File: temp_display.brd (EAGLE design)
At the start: 101.6 x 76.2 mm, 66 parts, among them IC2 ATMEGA168PROUND, Q1 2N2907, T1 BC547

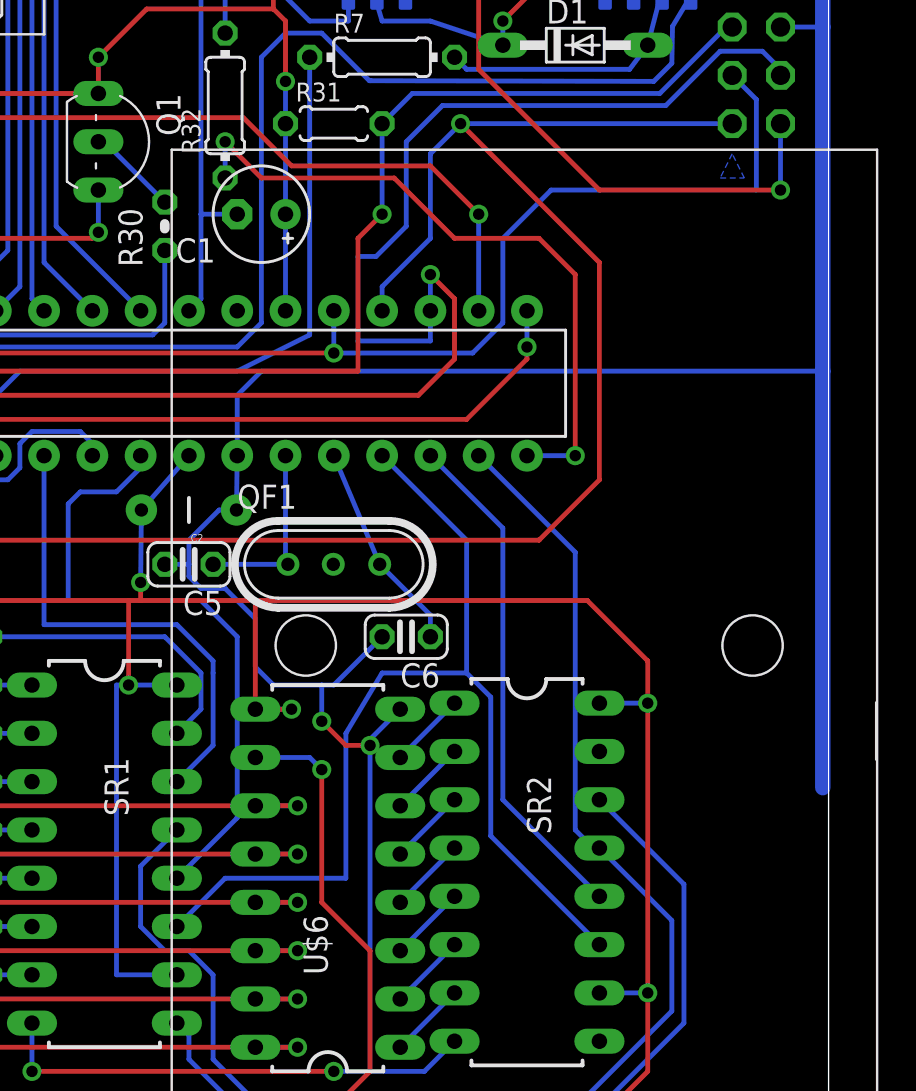
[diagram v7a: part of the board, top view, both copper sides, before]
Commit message: Now shutting down the display during isploading. But the system isn't stable anymore.
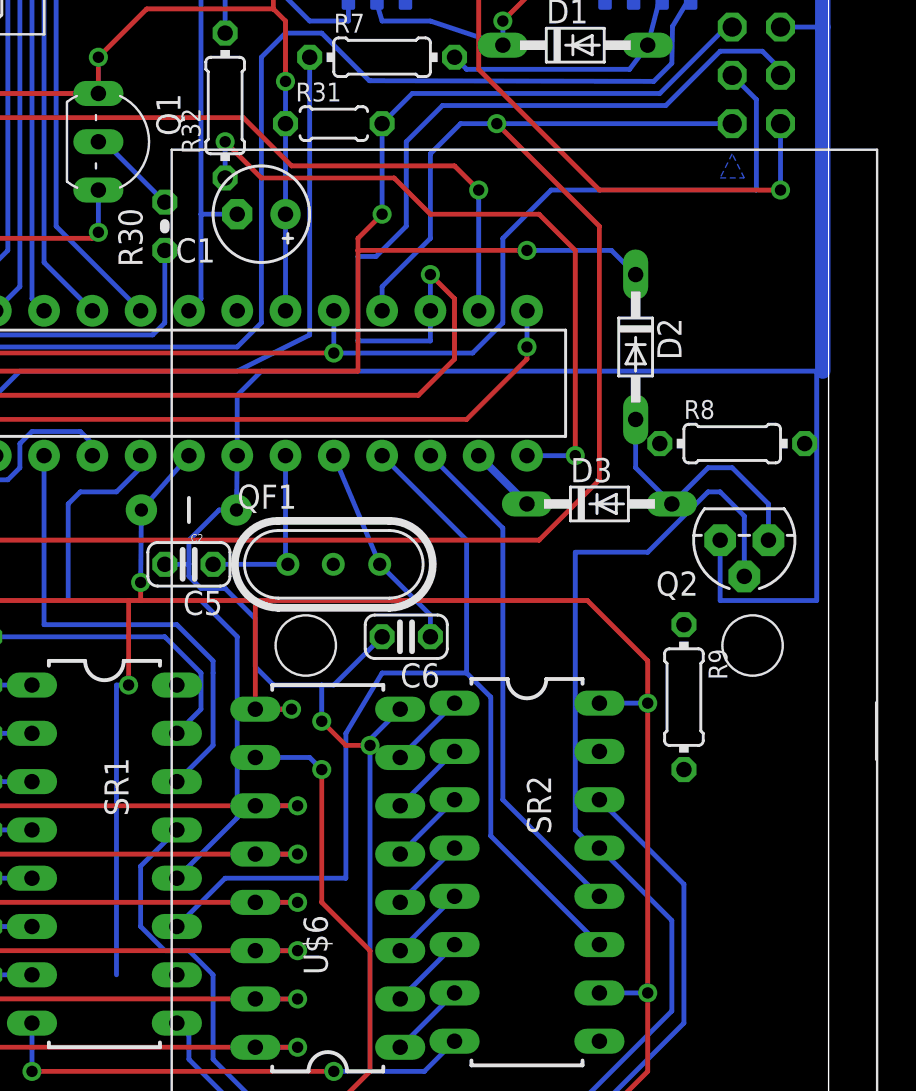
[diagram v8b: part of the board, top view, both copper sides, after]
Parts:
- added D2, D3: BAS15, diode:DO34-7
- added Q2: FQN1N50C, adafruit:TO92
- added R8, R9: 10K, resistor:0204/7
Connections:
- new net N$13: D3.C, IC2.13
- new net N$14: D2.A, D3.A, Q2.1, R8.2
- net +5: no longer SR1.10, SR1.16
- net +5V: now also R8.1, R9.1, SR1.10, SR1.16
- net GND: now also Q2.3
- net OE: now also Q2.2, R9.2; no longer IC2.13
- net RESET: now also D2.C
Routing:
- net RESET: track 62.6 -> 77.8 mm, vias 2 -> 3
- net N$14: track 0.00 -> 13.8 mm
- net OE: track 75.5 -> 82.3 mm
- net +5: track 386.0 -> 380.3 mm
- net N$13: track 0.00 -> 3.59 mm
- net GND: track 473.0 -> 471.4 mm
- net N$27: track 102.9 -> 102.1 mm
- net N$5: track 54.8 -> 55.5 mm
- net BTH_PW_TRANS: track 35.3 -> 36.0 mm
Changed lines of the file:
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@@
 <element name="C5" library="resistor" package="C025-024X044" value="" x="67.945" y="30.48" rot="R180"/>
 <element name="C6" library="resistor" package="C025-024X044" value="" x="79.375" y="26.67" rot="R180"/>
+<element name="D2" library="diode" package="DO34-7" value="BAS15" x="91.44" y="41.91" rot="R270"/>
+<element name="D3" library="diode" package="DO34-7" value="BAS15" x="89.535" y="33.655"/>
+<element name="R8" library="resistor" package="0204/7" value="10K" x="96.52" y="36.83"/>
+<element name="Q2" library="adafruit" package="TO92" value="FQN1N50C" x="97.155" y="31.75" rot="R180"/>
+<element name="R9" library="resistor" package="0204/7" value="10K" x="93.98" y="23.495" rot="R270"/>
 </elements>
 <signals>
@@
 <via x="52.705" y="40.64" extent="1-16" drill="0.6" shape="square"/>
 <wire x1="52.705" y1="40.64" x2="76.835" y2="40.64" width="0.254" layer="1"/>
-<wire x1="76.835" y1="40.64" x2="76.835" y2="47.625" width="0.254" layer="1"/>
+<wire x1="76.835" y1="40.64" x2="76.835" y2="46.99" width="0.254" layer="1"/>
+<wire x1="76.835" y1="46.99" x2="76.835" y2="47.625" width="0.254" layer="1"/>
 <wire x1="76.835" y1="47.625" x2="78.105" y2="48.895" width="0.254" layer="1"/>
 <via x="78.105" y="48.895" extent="1-16" drill="0.6" shape="square"/>
@@
 <wire x1="92.71" y1="55.245" x2="96.2025" y2="58.7375" width="0.254" layer="16"/>
 <wire x1="96.2025" y1="58.7375" x2="96.52" y2="58.7375" width="0.254" layer="16"/>
+<contactref element="D2" pad="C"/>
+<wire x1="76.835" y1="46.99" x2="85.725" y2="46.99" width="0.254" layer="1"/>
+<via x="85.725" y="46.99" extent="1-16" drill="0.6" shape="square"/>
+<wire x1="85.725" y1="46.99" x2="90.17" y2="46.99" width="0.254" layer="16"/>
+<wire x1="90.17" y1="46.99" x2="91.44" y2="45.72" width="0.254" layer="16"/>
 </signal>
 <signal name="SERIAL_RX">
@@
 <wire x1="42.8625" y1="26.3906" x2="42.9006" y2="26.4287" width="0.254" layer="16"/>
 <wire x1="42.9006" y1="22.8219" x2="42.8625" y2="22.86" width="0.254" layer="16"/>
-<wire x1="96.52" y1="53.6575" x2="82.2325" y2="53.6575" width="0.254" layer="16"/>
+<wire x1="96.52" y1="53.6575" x2="84.1375" y2="53.6575" width="0.254" layer="16"/>
+<wire x1="84.1375" y1="53.6575" x2="82.2325" y2="53.6575" width="0.254" layer="16"/>
 <wire x1="82.2325" y1="53.6575" x2="80.645" y2="52.07" width="0.254" layer="16"/>
 <wire x1="80.645" y1="52.07" x2="80.645" y2="47.625" width="0.254" layer="16"/>
 <wire x1="80.645" y1="47.625" x2="78.105" y2="45.085" width="0.254" layer="16"/>
-<via x="82.2325" y="53.6575" extent="1-16" drill="0.6" shape="square"/>
-<wire x1="82.2325" y1="53.6575" x2="89.535" y2="46.355" width="0.254" layer="1"/>
-<wire x1="89.535" y1="46.355" x2="89.535" y2="34.925" width="0.254" layer="1"/>
+<via x="84.1375" y="53.6575" extent="1-16" drill="0.6" shape="square"/>
+<wire x1="84.1375" y1="53.6575" x2="89.535" y2="48.26" width="0.254" layer="1"/>
+<wire x1="89.535" y1="48.26" x2="89.535" y2="34.925" width="0.254" layer="1"/>
 <wire x1="89.535" y1="34.925" x2="86.36" y2="31.75" width="0.254" layer="1"/>
 <wire x1="86.36" y1="31.75" x2="51.7525" y2="31.75" width="0.254" layer="1"/>
@@
 <wire x1="101.2825" y1="75.2475" x2="101.2825" y2="58.7375" width="0.8128" layer="16"/>
 <wire x1="101.2825" y1="58.7375" x2="101.2825" y2="40.64" width="0.8128" layer="16"/>
-<wire x1="101.2825" y1="40.64" x2="101.2825" y2="18.7325" width="0.8128" layer="16"/>
 <wire x1="70.485" y1="36.195" x2="70.485" y2="39.37" width="0.254" layer="16"/>
 <wire x1="70.485" y1="39.37" x2="71.755" y2="40.64" width="0.254" layer="16"/>
-<wire x1="71.755" y1="40.64" x2="101.2825" y2="40.64" width="0.254" layer="16"/>
+<wire x1="71.755" y1="40.64" x2="100.965" y2="40.64" width="0.254" layer="16"/>
 <contactref element="T1" pad="1"/>
 <contactref element="TM1" pad="S"/>
+<wire x1="100.965" y1="40.64" x2="101.2825" y2="40.64" width="0.254" layer="16"/>
 <wire x1="70.8025" y1="71.755" x2="70.8025" y2="74.93" width="0.254" layer="16"/>
 <wire x1="70.8025" y1="74.93" x2="69.85" y2="75.2475" width="0.254" layer="16"/>
@@
 <wire x1="75.565" y1="24.13" x2="74.93" y2="24.13" width="0.254" layer="16"/>
 <wire x1="66.675" y1="30.48" x2="67.945" y2="30.48" width="0.254" layer="16"/>
+<contactref element="Q2" pad="3"/>
+<wire x1="95.885" y1="31.75" x2="95.885" y2="28.575" width="0.254" layer="16"/>
+<wire x1="95.885" y1="28.575" x2="100.965" y2="28.575" width="0.254" layer="16"/>
+<wire x1="100.965" y1="28.575" x2="100.965" y2="40.64" width="0.254" layer="16"/>
 </signal>
 <signal name="STCP1">
@@
 <wire x1="93.345" y1="6.985" x2="93.345" y2="11.7475" width="0.254" layer="16"/>
 <wire x1="93.345" y1="11.7475" x2="89.535" y2="15.5575" width="0.254" layer="16"/>
-<contactref element="IC2" pad="13"/>
-<wire x1="88.265" y1="31.115" x2="83.185" y2="36.195" width="0.254" layer="16"/>
 <wire x1="89.535" y1="15.5575" x2="89.2175" y2="15.5575" width="0.254" layer="16"/>
 <wire x1="89.2175" y1="15.5575" x2="88.265" y2="16.51" width="0.254" layer="16"/>
 <wire x1="88.265" y1="16.51" x2="88.265" y2="31.115" width="0.254" layer="16"/>
+<contactref element="Q2" pad="2"/>
+<contactref element="R9" pad="2"/>
+<wire x1="97.155" y1="29.845" x2="97.155" y2="33.02" width="0.254" layer="16"/>
+<wire x1="97.155" y1="33.02" x2="95.885" y2="34.29" width="0.254" layer="16"/>
+<wire x1="95.885" y1="34.29" x2="95.25" y2="34.29" width="0.254" layer="16"/>
+<wire x1="95.25" y1="34.29" x2="92.075" y2="31.115" width="0.254" layer="16"/>
+<wire x1="92.075" y1="31.115" x2="88.265" y2="31.115" width="0.254" layer="16"/>
+<wire x1="89.535" y1="15.5575" x2="93.98" y2="19.685" width="0" layer="19" extent="1-1"/>
 </signal>
 <signal name="STCP2">
@@
 <wire x1="85.725" y1="36.195" x2="88.265" y2="36.195" width="0.254" layer="16"/>
 <via x="88.265" y="36.195" extent="1-16" drill="0.6" shape="square"/>
-<wire x1="88.265" y1="36.195" x2="88.265" y2="45.72" width="0.254" layer="1"/>
-<wire x1="88.265" y1="45.72" x2="86.36" y2="47.625" width="0.254" layer="1"/>
-<wire x1="86.36" y1="47.625" x2="81.915" y2="47.625" width="0.254" layer="1"/>
-<wire x1="81.915" y1="47.625" x2="78.74" y2="50.8" width="0.254" layer="1"/>
+<wire x1="88.265" y1="36.195" x2="88.265" y2="46.99" width="0.254" layer="1"/>
+<wire x1="88.265" y1="46.99" x2="86.36" y2="48.895" width="0.254" layer="1"/>
+<wire x1="86.36" y1="48.895" x2="80.645" y2="48.895" width="0.254" layer="1"/>
+<wire x1="80.645" y1="48.895" x2="78.74" y2="50.8" width="0.254" layer="1"/>
 <wire x1="78.74" y1="50.8" x2="71.755" y2="50.8" width="0.254" layer="1"/>
 <wire x1="71.755" y1="50.8" x2="69.85" y2="52.705" width="0.254" layer="1"/>
@@
 <wire x1="0" y1="23.495" x2="1.27" y2="23.495" width="0.254" layer="1"/>
 <wire x1="1.27" y1="23.495" x2="1.27" y2="23.46325" width="0.254" layer="1"/>
-<contactref element="SR1" pad="16"/>
-<contactref element="SR1" pad="10"/>
 <wire x1="1.27" y1="23.46325" x2="1.27" y2="17.78" width="0.254" layer="1"/>
 <wire x1="1.27" y1="17.78" x2="17.78" y2="1.27" width="0.254" layer="1"/>
 <wire x1="17.78" y1="1.27" x2="89.535" y2="1.27" width="0.254" layer="1"/>
 <wire x1="64.135" y1="8.89" x2="64.135" y2="24.13" width="0.254" layer="16"/>
-<wire x1="64.77" y1="24.13" x2="67.31" y2="24.13" width="0.254" layer="16"/>
-<wire x1="67.31" y1="8.89" x2="64.135" y2="8.89" width="0.254" layer="16"/>
 <contactref element="SR2" pad="16"/>
 <contactref element="SR2" pad="10"/>
@@
 <contactref element="S2" pad="2"/>
 <contactref element="IC2" pad="16"/>
-<wire x1="83.185" y1="43.815" x2="83.185" y2="48.895" width="0.254" layer="16"/>
-<via x="83.185" y="48.895" extent="1-16" drill="0.6" shape="square"/>
-<wire x1="83.185" y1="48.895" x2="80.645" y2="51.435" width="0.254" layer="1"/>
-<wire x1="80.645" y1="51.435" x2="73.3425" y2="51.435" width="0.254" layer="1"/>
+<wire x1="83.185" y1="43.815" x2="83.185" y2="50.165" width="0.254" layer="16"/>
+<via x="83.185" y="50.165" extent="1-16" drill="0.6" shape="square"/>
+<wire x1="83.185" y1="50.165" x2="81.915" y2="51.435" width="0.254" layer="1"/>
+<wire x1="81.915" y1="51.435" x2="73.3425" y2="51.435" width="0.254" layer="1"/>
 <wire x1="73.3425" y1="51.435" x2="70.8025" y2="53.975" width="0.254" layer="1"/>
 <wire x1="70.8025" y1="53.975" x2="45.72" y2="53.975" width="0.254" layer="1"/>
@@
 <contactref element="JP8" pad="1"/>
 <wire x1="64.135" y1="68.58" x2="64.135" y2="71.755" width="0.254" layer="16"/>
+<contactref element="R8" pad="1"/>
+<contactref element="R9" pad="1"/>
+<contactref element="SR1" pad="16"/>
+<contactref element="SR1" pad="10"/>
+<wire x1="92.71" y1="36.83" x2="64.135" y2="68.58" width="0" layer="19" extent="1-1"/>
+<wire x1="93.98" y1="27.305" x2="92.71" y2="36.83" width="0" layer="19" extent="1-1"/>
+<wire x1="67.31" y1="24.13" x2="93.98" y2="27.305" width="0" layer="19" extent="1-1"/>
+<wire x1="67.31" y1="8.89" x2="67.31" y2="24.13" width="0" layer="19" extent="1-1"/>
 </signal>
 <signal name="N$8">
@@
 <wire x1="80.645" y1="27.813" x2="80.645" y2="26.67" width="0.254" layer="16"/>
 </signal>
+<signal name="N$13">
+<contactref element="IC2" pad="13"/>
+<contactref element="D3" pad="C"/>
+<wire x1="83.185" y1="36.195" x2="85.725" y2="33.655" width="0.4064" layer="16"/>
+</signal>
+<signal name="N$14">
+<contactref element="D2" pad="A"/>
+<contactref element="R8" pad="2"/>
+<contactref element="D3" pad="A"/>
+<contactref element="Q2" pad="1"/>
+<wire x1="91.44" y1="38.1" x2="91.44" y2="35.56" width="0.254" layer="16"/>
+<wire x1="91.44" y1="35.56" x2="93.345" y2="33.655" width="0.254" layer="16"/>
+<wire x1="98.425" y1="31.75" x2="98.425" y2="33.655" width="0.254" layer="16"/>
+<wire x1="98.425" y1="33.655" x2="96.52" y2="35.56" width="0.254" layer="16"/>
+<wire x1="96.52" y1="35.56" x2="95.25" y2="35.56" width="0.254" layer="16"/>
+<wire x1="95.25" y1="35.56" x2="93.345" y2="33.655" width="0.254" layer="16"/>
+<wire x1="98.425" y1="33.655" x2="100.33" y2="36.83" width="0" layer="19" extent="16-16"/>
+</signal>
 </signals>
